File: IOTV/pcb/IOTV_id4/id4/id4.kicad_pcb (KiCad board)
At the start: 2 copper layers, 109.2 x 73.7 mm, 57 parts, among them Q1 S8050, Q10 S8050, Q11 S8050, Q12 S8050, Q13 S8050, Q14 S8050, Q15 S8050, Q2 S8050, Q3 S8050, Q4 S8050, Q5 S8050, Q6 S8050, Q7 S8050, Q8 S8050, Q9 S8050, SW1 SW_Push, SW2 SW_Push, SW3 SW_Push, U1 ESP32_DevKit_V1_DOIT, U2 DFR0299

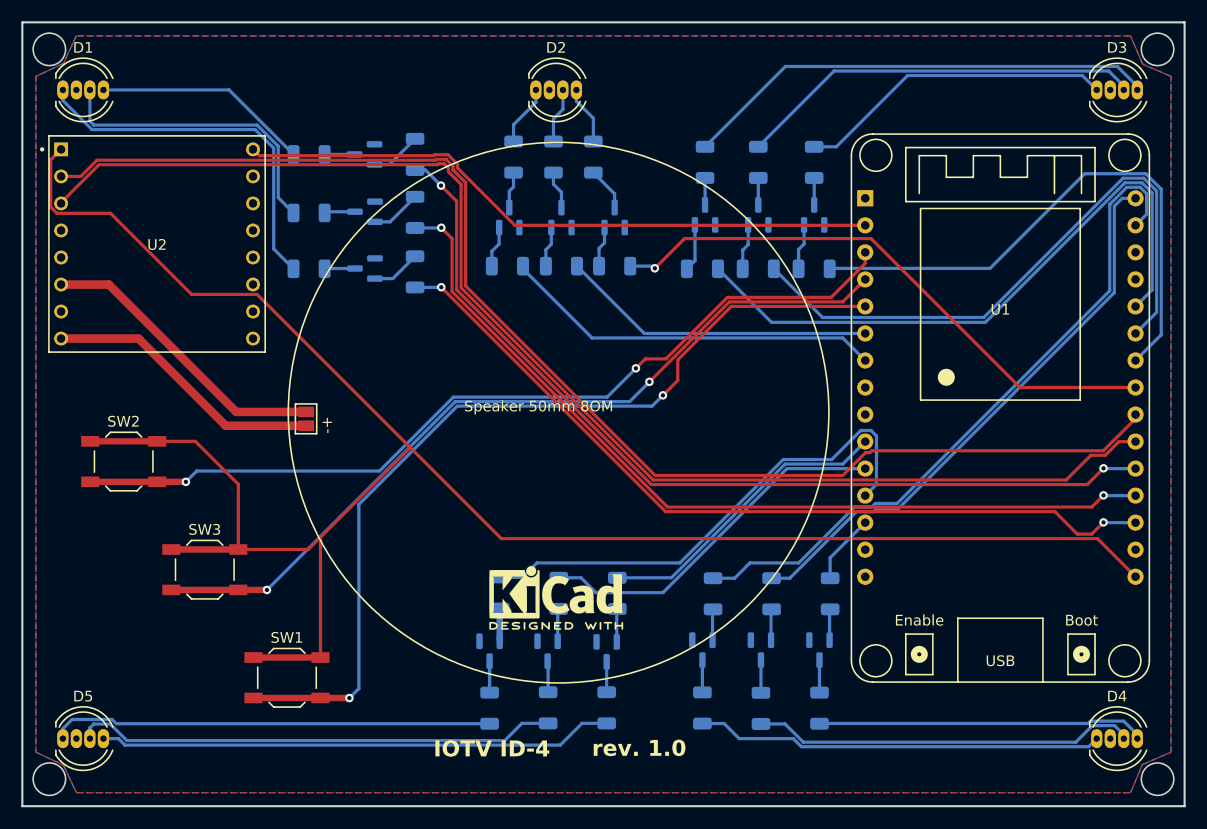
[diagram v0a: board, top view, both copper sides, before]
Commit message: PCB id4 кнопки на землю
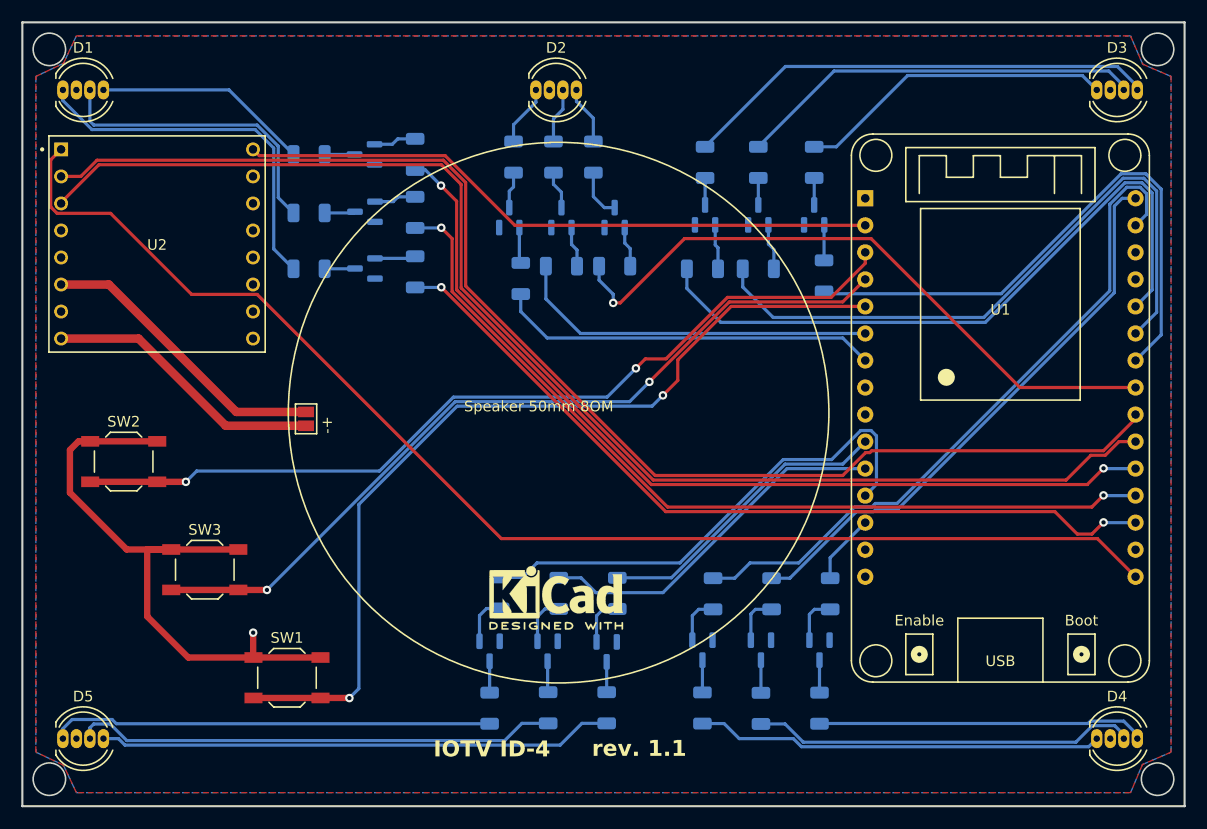
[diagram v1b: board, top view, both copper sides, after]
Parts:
- moved R22 1.71 mm to (163.7, 77.4), turned to 90 degrees
- moved R16 1.14 mm to (192.2, 77.2), turned to 90 degrees
- turned R17 to 0 degrees
- turned R18 to 0 degrees
- turned R23 to 0 degrees
- turned R24 to 0 degrees
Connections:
- Q1 pad 1: GND -> Net-(Q1-B)
- Q1 pad 2: Net-(Q1-B) -> GND
- Q10 pad 1: GND -> Net-(Q10-B)
- Q10 pad 2: Net-(Q10-B) -> GND
- Q11 pad 1: GND -> Net-(Q11-B)
- Q11 pad 2: Net-(Q11-B) -> GND
- Q12 pad 1: GND -> Net-(Q12-B)
- Q12 pad 2: Net-(Q12-B) -> GND
- Q13 pad 1: GND -> Net-(Q13-B)
- Q13 pad 2: Net-(Q13-B) -> GND
- Q14 pad 1: GND -> Net-(Q14-B)
- Q14 pad 2: Net-(Q14-B) -> GND
- Q15 pad 1: GND -> Net-(Q15-B)
- Q15 pad 2: Net-(Q15-B) -> GND
- Q2 pad 1: GND -> Net-(Q2-B)
- Q2 pad 2: Net-(Q2-B) -> GND
- Q3 pad 1: GND -> Net-(Q3-B)
- Q3 pad 2: Net-(Q3-B) -> GND
- Q4 pad 1: GND -> Net-(Q4-B)
- Q4 pad 2: Net-(Q4-B) -> GND
- Q5 pad 1: GND -> Net-(Q5-B)
- Q5 pad 2: Net-(Q5-B) -> GND
- Q6 pad 1: GND -> Net-(Q6-B)
- Q6 pad 2: Net-(Q6-B) -> GND
- Q7 pad 1: GND -> Net-(Q7-B)
- Q7 pad 2: Net-(Q7-B) -> GND
- Q8 pad 1: GND -> Net-(Q8-B)
- Q8 pad 2: Net-(Q8-B) -> GND
- Q9 pad 1: GND -> Net-(Q9-B)
- Q9 pad 2: Net-(Q9-B) -> GND
- SW1 pad 1: VCC_3.3 -> GND
- SW2 pad 1: VCC_3.3 -> GND
- SW3 pad 1: VCC_3.3 -> GND
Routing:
- net VCC_3.3: track 187.9 -> 122.2 mm
- net GND: track 0.00 -> 59.4 mm, vias 0 -> 1
- net GPIO_5: track 54.5 -> 61.4 mm
- net GPIO_32: track 29.7 -> 34.4 mm
- net GPIO_21: track 60.0 -> 64.0 mm
- net GPIO_19: track 58.0 -> 61.9 mm
- net Net-(Q5-B): track 2.92 -> 4.59 mm
- net Net-(Q6-B): track 2.92 -> 4.57 mm
- net GPIO_18: track 52.6 -> 54.1 mm
- net Net-(Q4-B): track 2.92 -> 4.50 mm
- net Net-(Q15-B): track 3.12 -> 4.67 mm
- net Net-(Q14-B): track 3.08 -> 4.62 mm
- net Net-(Q13-B): track 3.10 -> 4.64 mm
- net Net-(Q7-B): track 4.34 -> 3.34 mm
- net Net-(Q2-B): track 4.81 -> 4.02 mm
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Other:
- board text added: "rev. 1.1"
- board text removed: "rev. 1.0"
